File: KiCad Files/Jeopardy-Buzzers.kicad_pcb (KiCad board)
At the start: 2 copper layers, 40 x 30 mm, 26 parts, among them J1 USB_C_Receptacle_USB2.0_14P, J2 Conn_01x02_Pin, J3 Conn_01x03_Socket, J4 Conn_01x03_Socket, J5 Conn_02x04_Odd_Even, U1 CH32V003FxUx, U2 CH340N, U3 NRF24L01_Breakout, U5 AMS1117-3.3, Y1 Crystal_24MHz

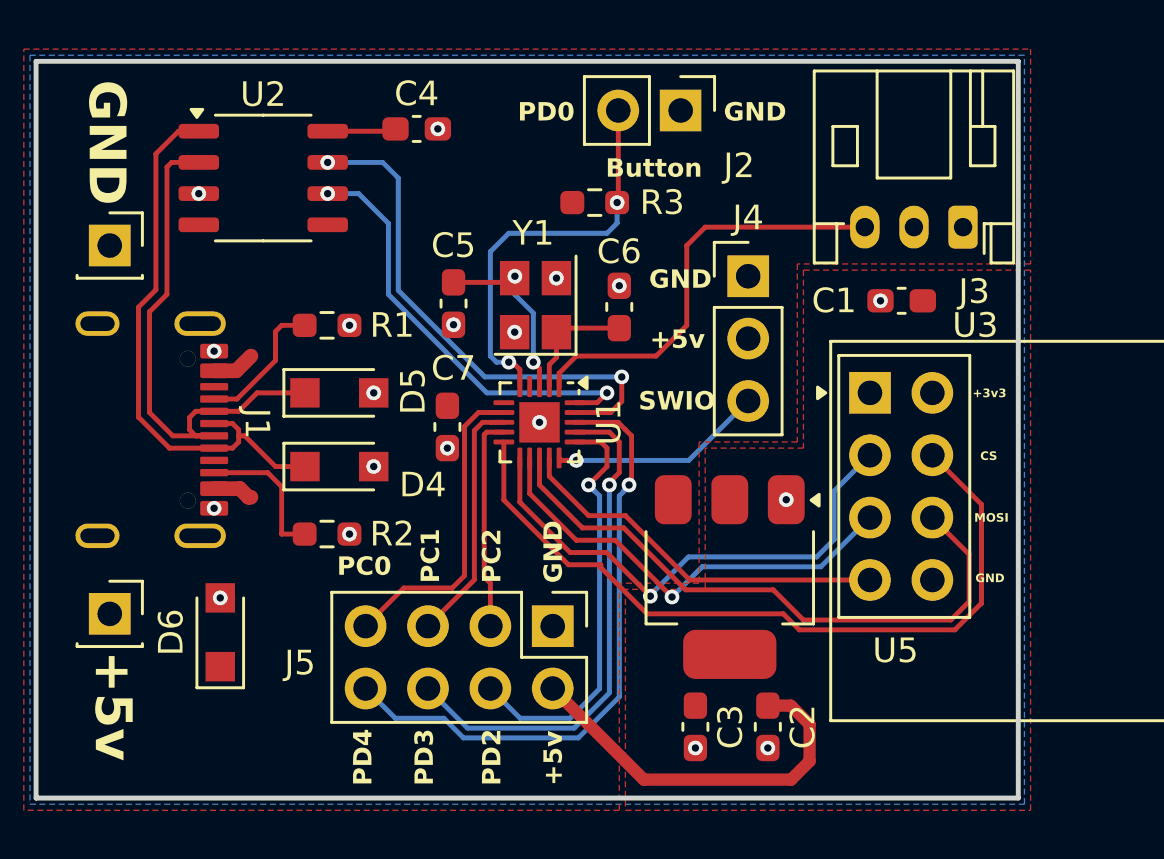
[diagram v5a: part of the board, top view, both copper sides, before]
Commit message: Added power led and user controlled led
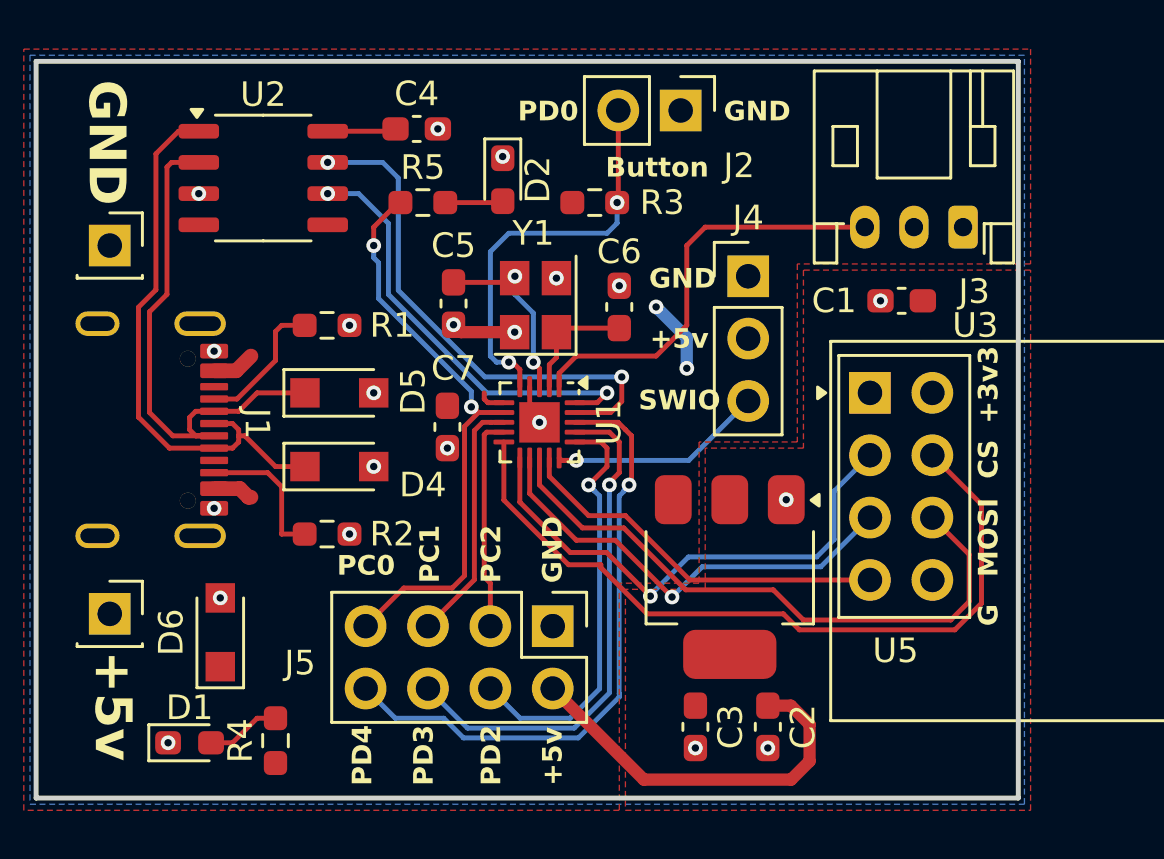
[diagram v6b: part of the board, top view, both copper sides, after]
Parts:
- added D1: LED, LED_SMD:LED_0603_1608Metric_Pad1.05x0.95mm_HandSolder, F.Cu at (26.2, 47.8)
- added D2: LED, LED_SMD:LED_0603_1608Metric_Pad1.05x0.95mm_HandSolder, F.Cu at (39.0, 24.8)
- added R4: 1k, Resistor_SMD:R_0603_1608Metric_Pad0.98x0.95mm_HandSolder, F.Cu at (29.8, 47.7)
- added R5: 1k, Resistor_SMD:R_0603_1608Metric_Pad0.98x0.95mm_HandSolder, F.Cu at (35.8, 25.8)
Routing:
- net MCU_PC0: track 13.3 -> 24.4 mm, vias 0 -> 2
- net GND: track 0.00 -> 4.23 mm, vias 19 -> 21
- net +5V: track 19.2 -> 23.3 mm, vias 0 -> 2
- net Net-(D1-A): track 0.00 -> 3.04 mm
- net Net-(D2-A): track 0.00 -> 2.37 mm
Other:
- board text added: "G"

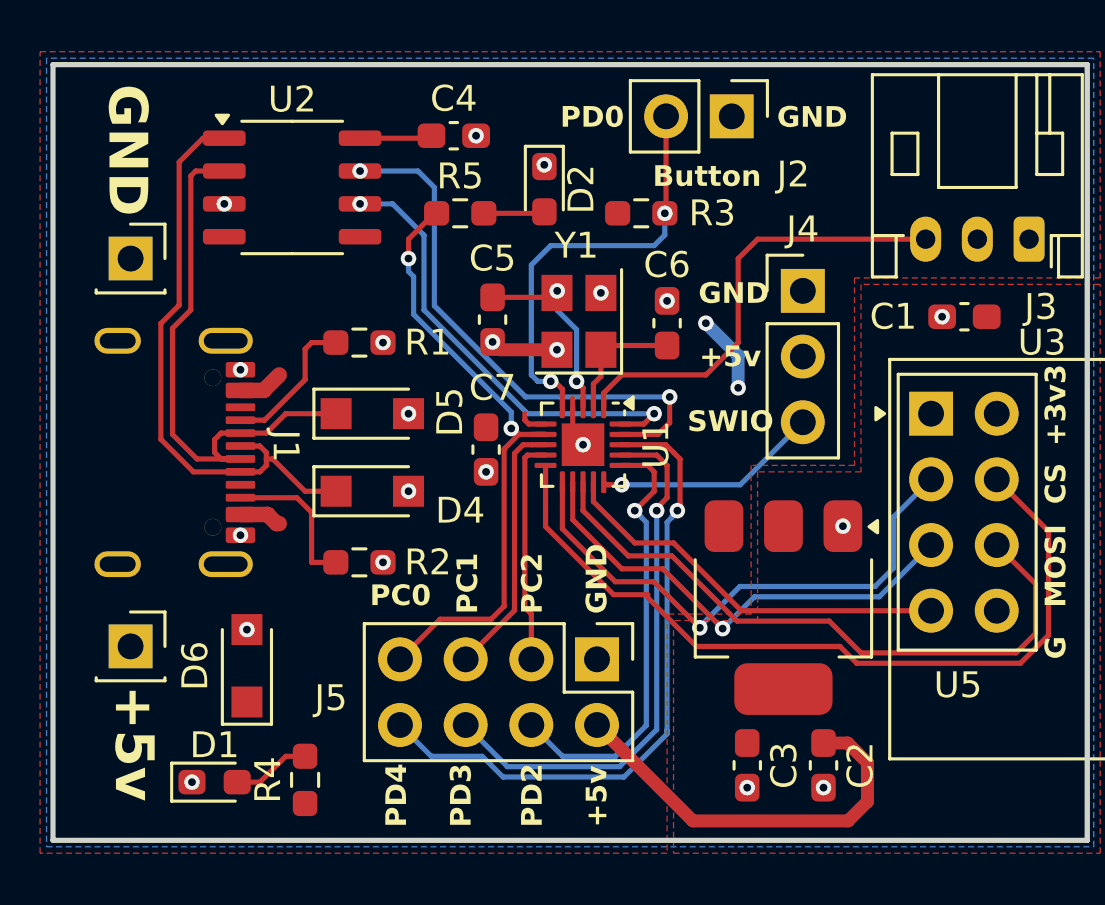
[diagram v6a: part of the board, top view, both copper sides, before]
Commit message: Moved Vias off of pads
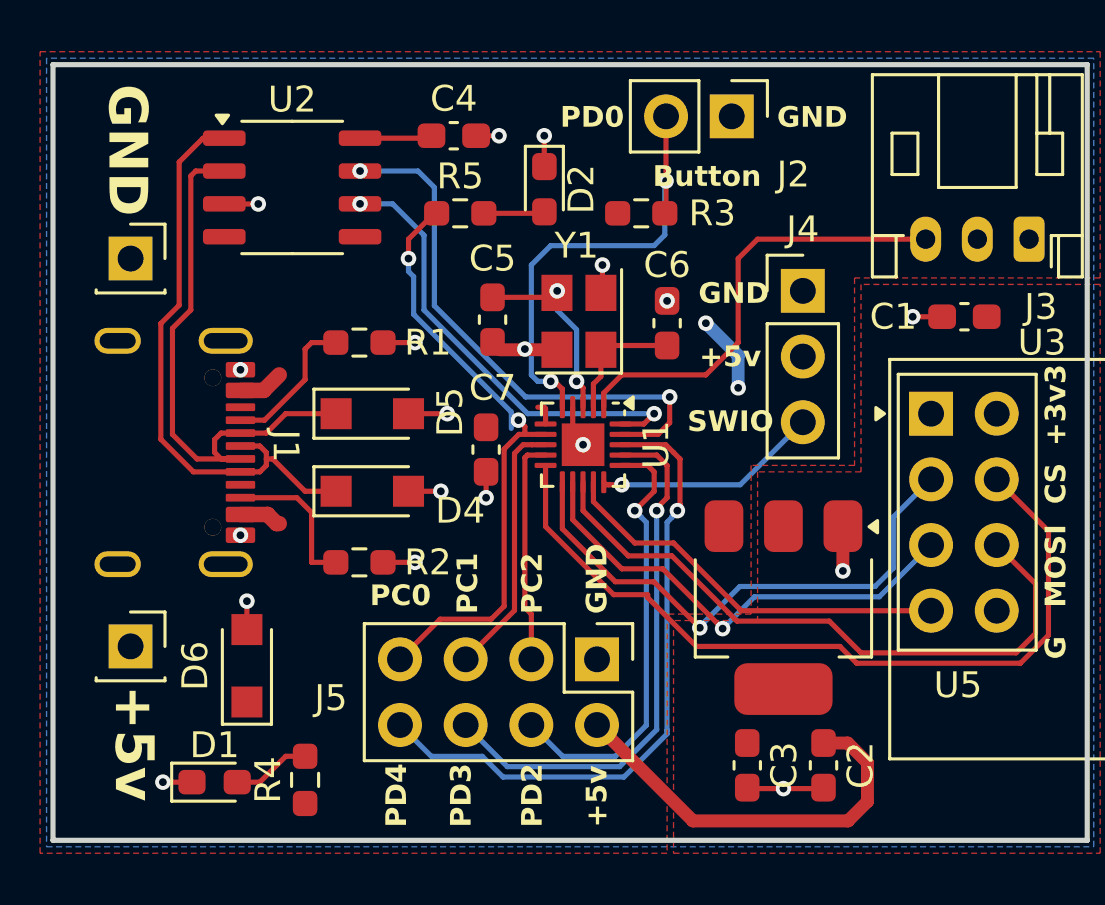
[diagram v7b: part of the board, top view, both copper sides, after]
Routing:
- net GND: track 4.23 -> 23.0 mm, vias 21 -> 19
- net Net-(J2-Pin_2): track 16.6 -> 17.9 mm

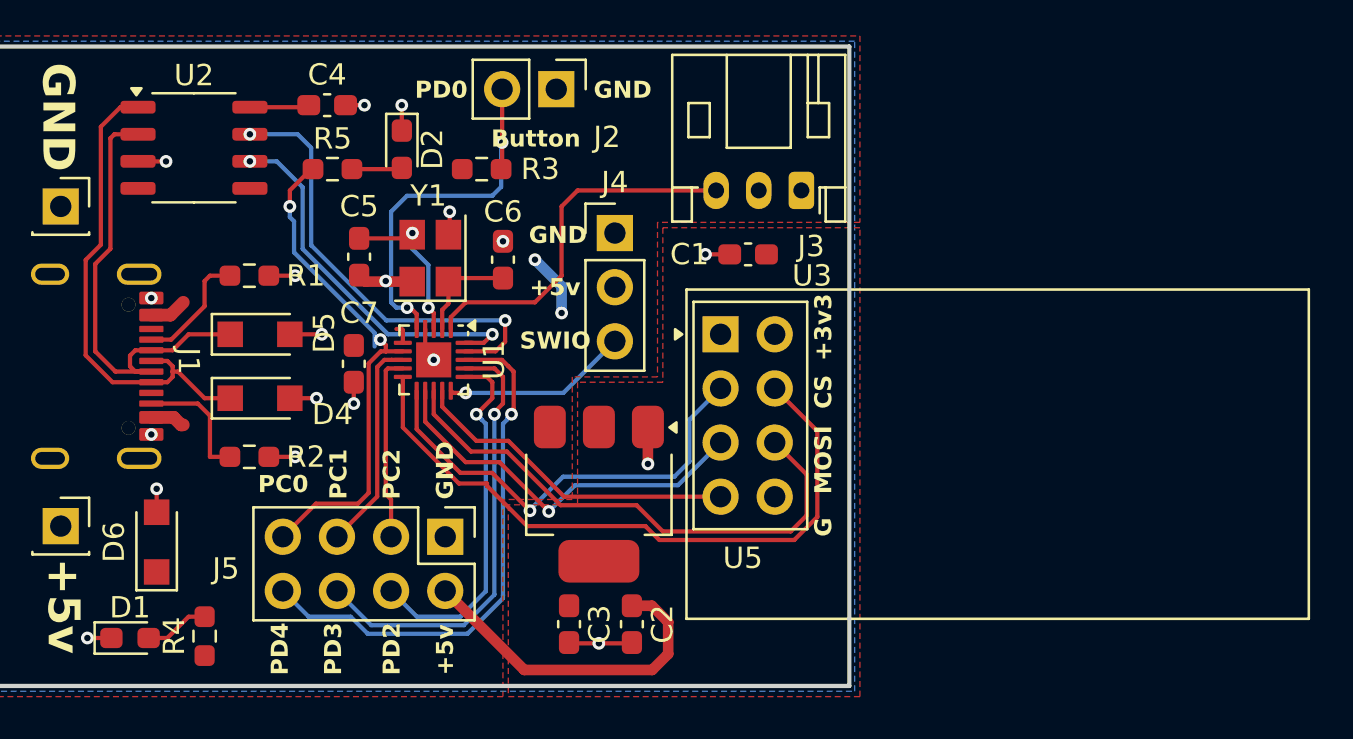
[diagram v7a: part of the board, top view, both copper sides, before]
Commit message: Updated LCSC Part Numbers
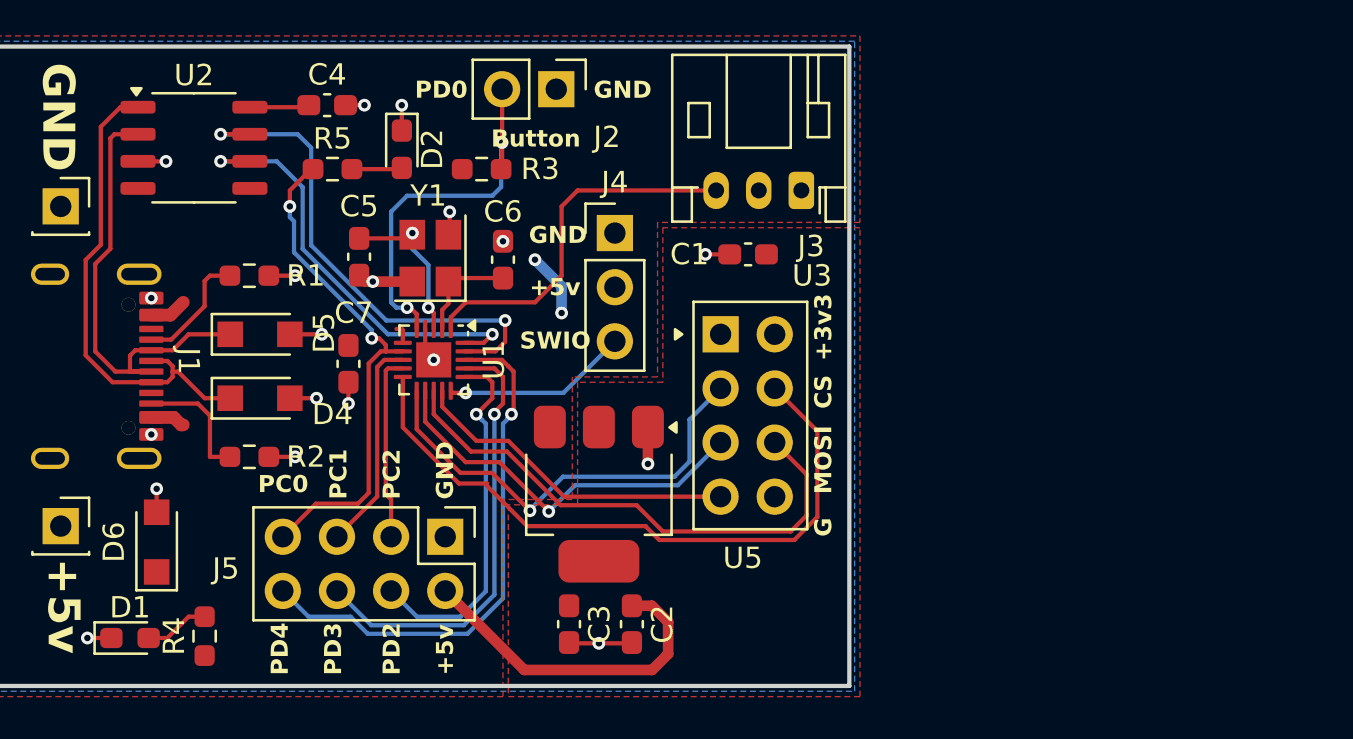
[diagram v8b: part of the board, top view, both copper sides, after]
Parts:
- moved C7 0.25 mm to (36.5, 34.9)
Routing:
- net MCU_UART_TX: track 21.4 -> 24.1 mm
- net MCU_UART_RX: track 17.9 -> 20.6 mm
